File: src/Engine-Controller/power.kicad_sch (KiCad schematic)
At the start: 51 parts, among them P1 EJ508A, P18 PPTC041LFBN-RC, P7 647676-2, U10 LMS8117AMP-3.3_NOPB, U2 LM22672MRE-5.0_NOPB, U3 LMS8117AMP-3.3_NOPB, U6 TPS2115APWR

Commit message: resolved all ERC schematic issues
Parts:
- C5: footprint Engine-Controller:CAP_EEEFP1E151AL -> Engine-Controller:EEEFP1E151AL
- P18: footprint CONN_4840.2201_SCH -> Engine-Controller:PPTC041LFBN-RC
- P7: footprint CONN_2043-1X04G00DAU_OUP -> Engine-Controller:647676-2
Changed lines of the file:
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@@
       (effects (font (size 1.27 1.27)) (justify left))
     )
-    (property "Footprint" "Engine-Controller:CAP_EEEFP1E151AL" (id 2) (at 128.905 52.705 0)
+    (property "Footprint" "Engine-Controller:EEEFP1E151AL" (id 2) (at 128.905 52.705 0)
       (effects (font (size 1.27 1.27)) hide)
     )
@@
     (pin "1")
   )
-  (symbol (lib_id "Engine-Controller:LMS8117AMP-3.3_NOPB") (at 117.475 92.71 0) (unit 1)
+  (symbol (lib_name "LMS8117AMP-3.3_NOPB_1") (lib_id "Engine-Controller:LMS8117AMP-3.3_NOPB") (at 117.475 92.71 0) (unit 1)
     (in_bom yes) (on_board yes)
     (property "Reference" "U3" (id 0) (at 117.475 87.63 0))
@@
       (effects (font (size 1.524 1.524)) hide)
     )
-    (property "Footprint" "CONN_4840.2201_SCH" (id 2) (at 263.525 116.84 0)
+    (property "Footprint" "Engine-Controller:PPTC041LFBN-RC" (id 2) (at 263.525 116.84 0)
       (effects (font (size 1.524 1.524)) hide)
     )
@@
       (effects (font (size 1.524 1.524)) hide)
     )
-    (property "Footprint" "CONN_2043-1X04G00DAU_OUP" (id 2) (at 52.07 180.34 0)
-      (effects (font (size 1.524 1.524)) hide)
-    )
+    (property "Footprint" "Engine-Controller:647676-2" (id 2) (at 52.07 180.34 0)
+      (effects (font (size 1.524 1.524)) hide)
+    )

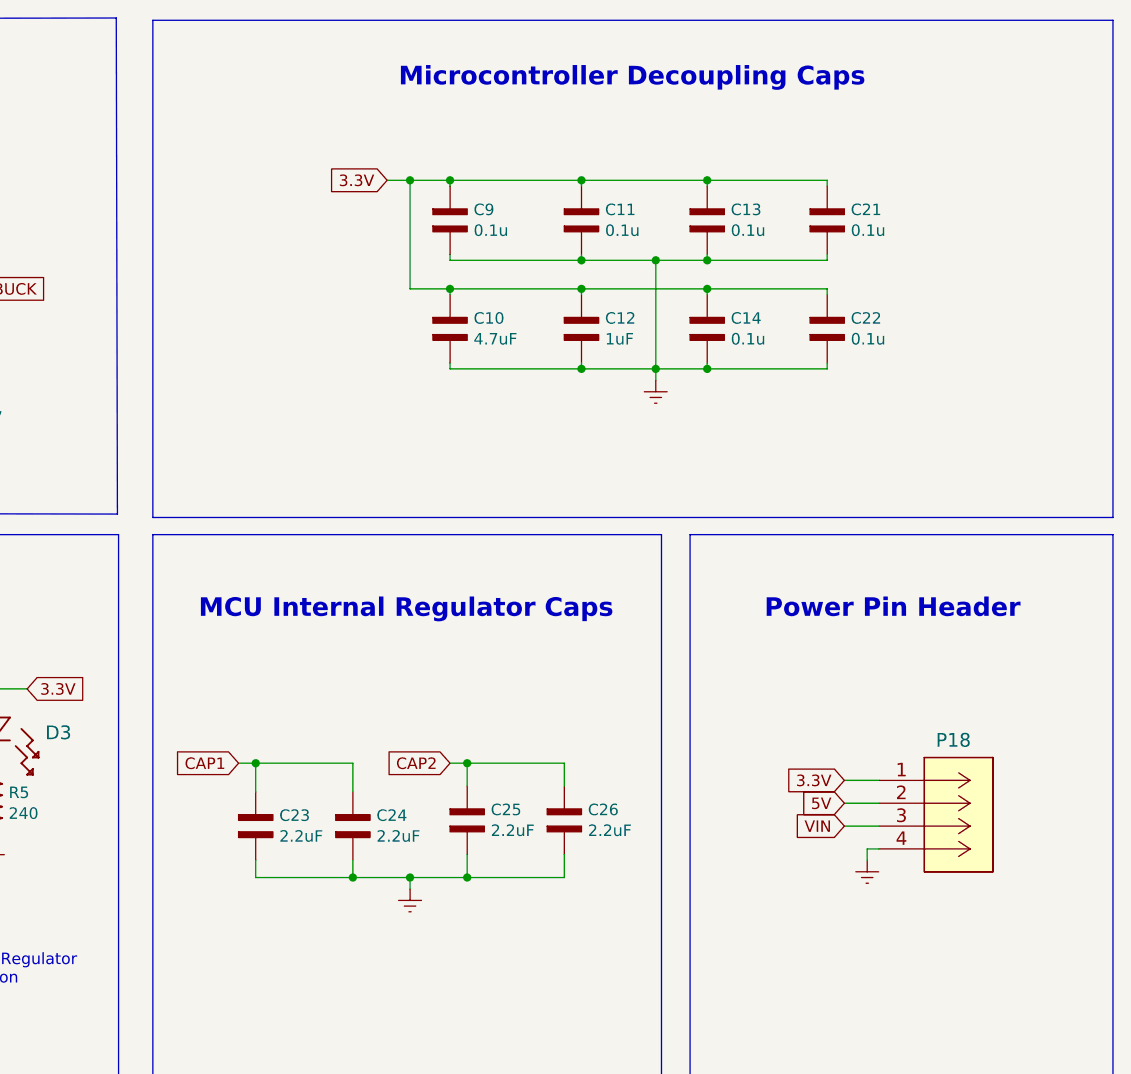
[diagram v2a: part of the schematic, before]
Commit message: removed uncessary caps from MCU LDO pins
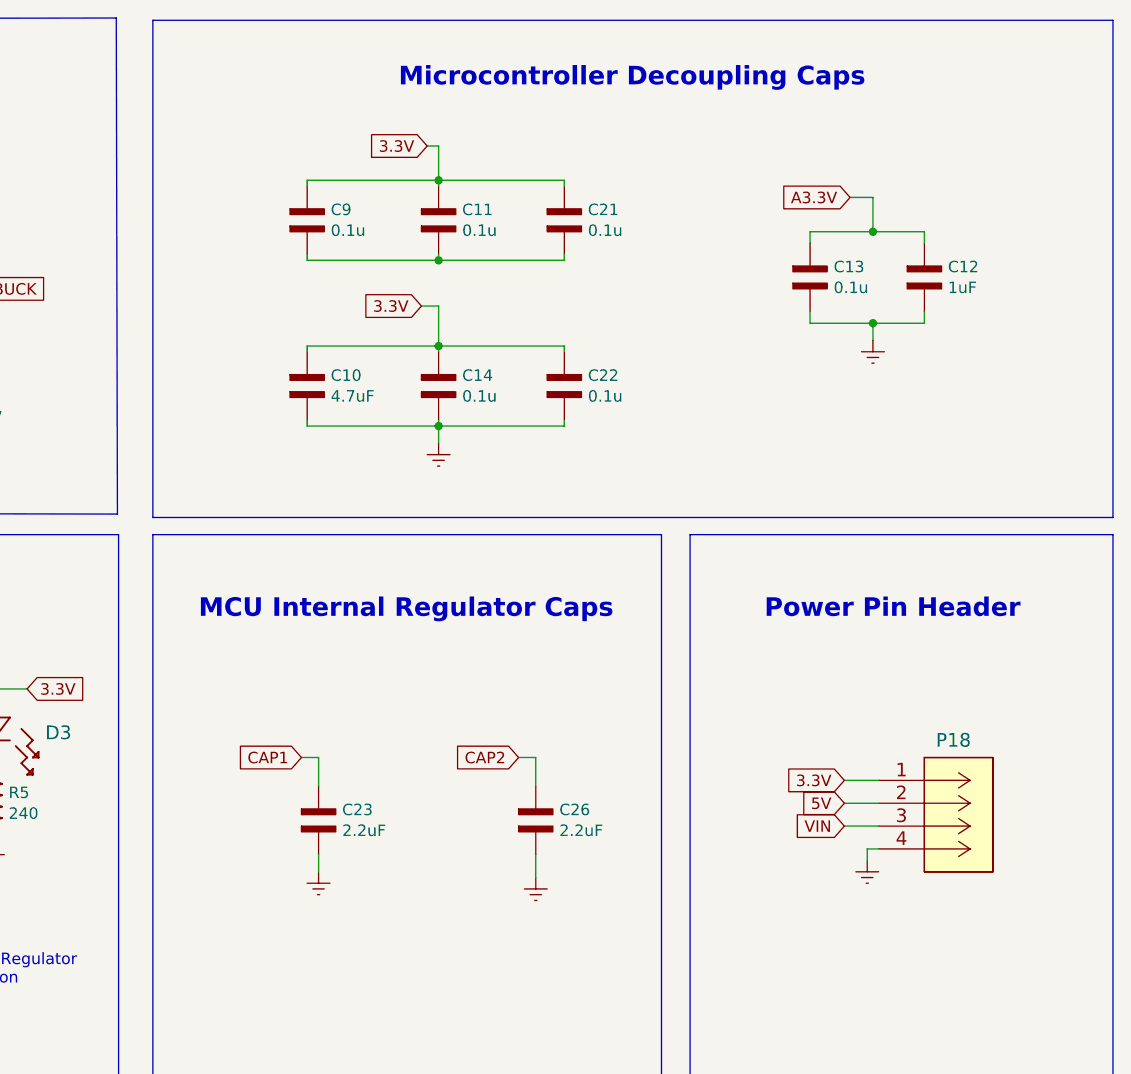
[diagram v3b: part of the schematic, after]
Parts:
- removed C24, C25: 2.2uF, Engine-Controller:CAP_0603, symbol Engine-Controller:CAP_0603
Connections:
- net 3.3V: no longer C12.2, C13.2
- net A3.3V: now also C12.2, C13.2
- net Earth: no longer C11.1, C21.1, C9.1
- new net: C11.1, C21.1, C9.1
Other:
- moved on the sheet: C10, C11, C12, C13, C14, C21, C22, C23, C26, C9

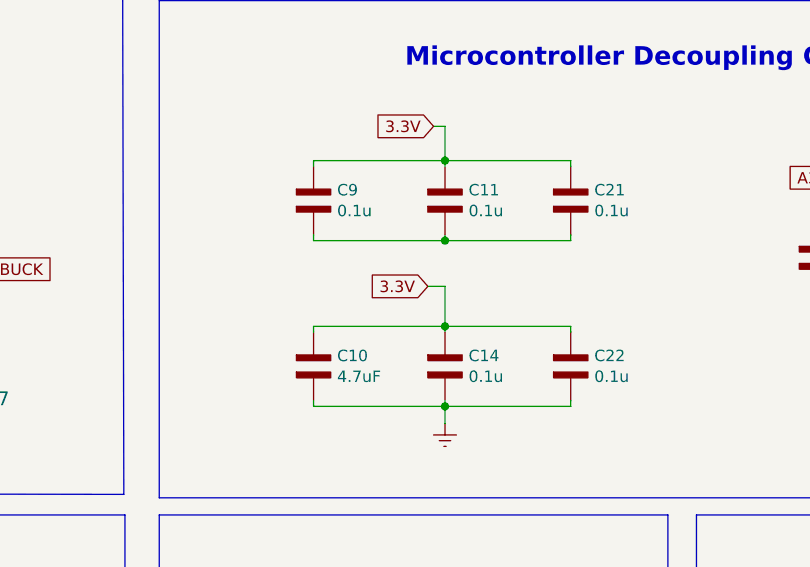
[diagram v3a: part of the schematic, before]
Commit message: removed uneccessary info from footprint lib files
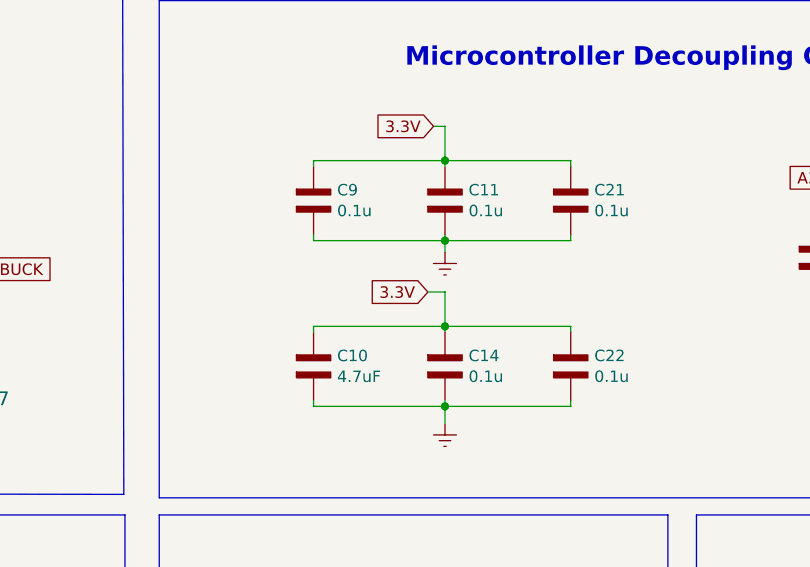
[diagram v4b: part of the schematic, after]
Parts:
- C27, C28, C6, C7: footprint Engine-Controller:CWR11HH106KB -> Engine-Controller:T491A106K010AT
- U10, U3: footprint Engine-Controller:SOT-223 -> Engine-Controller:LMS8117AMP-3.3NOPB
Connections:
- net Earth: now also C11.1, C21.1, C9.1
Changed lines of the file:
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@@
     (stroke (width 0) (type default) (color 0 0 0 0))
   )
-  (wire (pts (xy 202.565 48.895) (xy 204.47 48.895))
+  (wire (pts (xy 202.565 49.53) (xy 204.47 49.53))
     (stroke (width 0) (type default) (color 0 0 0 0))
   )
@@
     (stroke (width 0) (type default) (color 0 0 0 0))
   )
+  (wire (pts (xy 204.47 43.815) (xy 204.47 45.085))
+    (stroke (width 0) (type default) (color 0 0 0 0))
+  )
   (wire (pts (xy 35.052 107.315) (xy 43.18 107.315))
     (stroke (width 0) (type default) (color 0 0 0 0))
@@
     (stroke (width 0) (type default) (color 0 0 0 0))
   )
-  (wire (pts (xy 204.47 48.895) (xy 204.47 53.34))
+  (wire (pts (xy 204.47 49.53) (xy 204.47 53.34))
     (stroke (width 0) (type default) (color 0 0 0 0))
   )
@@
     )
   )
-  (global_label "3.3V" (shape input) (at 202.565 48.895 180) (fields_autoplaced)
-    (effects (font (size 1.27 1.27)) (justify right))
-    (property "Intersheet References" "${INTERSHEET_REFS}" (id 0) (at 132.08 20.32 0)
+  (global_label "3.3V" (shape input) (at 202.565 49.53 180) (fields_autoplaced)
+    (effects (font (size 1.27 1.27)) (justify right))
+    (property "Intersheet References" "${INTERSHEET_REFS}" (id 0) (at 132.08 20.955 0)
       (effects (font (size 1.27 1.27)) hide)
     )
@@
       (effects (font (size 1.524 1.524)) (justify left))
     )
-    (property "Footprint" "Engine-Controller:CWR11HH106KB" (id 2) (at 98.171 95.885 0)
+    (property "Footprint" "Engine-Controller:T491A106K010AT" (id 2) (at 98.171 95.885 0)
       (effects (font (size 1.524 1.524)) hide)
     )
@@
       (effects (font (size 1.524 1.524)) (justify left))
     )
-    (property "Footprint" "Engine-Controller:CWR11HH106KB" (id 2) (at 119.126 95.885 0)
+    (property "Footprint" "Engine-Controller:T491A106K010AT" (id 2) (at 119.126 95.885 0)
       (effects (font (size 1.524 1.524)) hide)
     )
@@
     (pin "1")
   )
-  (symbol (lib_name "LMS8117AMP-3.3_NOPB_1") (lib_id "Engine-Controller:LMS8117AMP-3.3_NOPB") (at 117.475 92.71 0) (unit 1)
+  (symbol (lib_id "Engine-Controller:LMS8117AMP-3.3_NOPB") (at 117.475 92.71 0) (unit 1)
     (in_bom yes) (on_board yes)
     (property "Reference" "U3" (id 0) (at 117.475 87.63 0))
@@
       (effects (font (size 1.27 1.27)) hide)
     )
-    (property "Footprint" "Engine-Controller:SOT-223" (id 2) (at 117.475 92.71 0)
+    (property "Footprint" "Engine-Controller:LMS8117AMP-3.3NOPB" (id 2) (at 117.475 92.71 0)
       (effects (font (size 1.27 1.27)) hide)
     )
@@
     )
     (property "Datasheet" "" (id 3) (at 252.095 110.49 0)
+      (effects (font (size 1.27 1.27)) hide)
+    )
+    (pin "1")
+  )
+  (symbol (lib_id "Engine-Controller:Earth") (at 204.47 45.085 0) (unit 1)
+    (in_bom yes) (on_board yes)
+    (property "Reference" "#PWR0111" (id 0) (at 204.47 51.435 0)
+      (effects (font (size 1.27 1.27)) hide)
+    )
+    (property "Value" "Earth" (id 1) (at 204.47 48.895 0)
+      (effects (font (size 1.27 1.27)) hide)
+    )
+    (property "Footprint" "" (id 2) (at 204.47 45.085 0)
+      (effects (font (size 1.27 1.27)) hide)
+    )
+    (property "Datasheet" "" (id 3) (at 204.47 45.085 0)
       (effects (font (size 1.27 1.27)) hide)
     )
@@
       (effects (font (size 1.524 1.524)) (justify left))
     )
-    (property "Footprint" "Engine-Controller:CWR11HH106KB" (id 2) (at 98.171 118.745 0)
+    (property "Footprint" "Engine-Controller:T491A106K010AT" (id 2) (at 98.171 118.745 0)
       (effects (font (size 1.524 1.524)) hide)
     )
@@
       (effects (font (size 1.27 1.27)) hide)
     )
-    (property "Footprint" "Engine-Controller:SOT-223" (id 2) (at 117.475 115.57 0)
+    (property "Footprint" "Engine-Controller:LMS8117AMP-3.3NOPB" (id 2) (at 117.475 115.57 0)
       (effects (font (size 1.27 1.27)) hide)
     )
@@
       (effects (font (size 1.524 1.524)) (justify left))
     )
-    (property "Footprint" "Engine-Controller:CWR11HH106KB" (id 2) (at 119.126 118.745 0)
+    (property "Footprint" "Engine-Controller:T491A106K010AT" (id 2) (at 119.126 118.745 0)
       (effects (font (size 1.524 1.524)) hide)
     )
@@
   (symbol (lib_id "Engine-Controller:Earth") (at 191.135 111.76 0) (unit 1)
     (in_bom yes) (on_board yes)
-    (property "Reference" "#PWR?" (id 0) (at 191.135 118.11 0)
+    (property "Reference" "#PWR0110" (id 0) (at 191.135 118.11 0)
       (effects (font (size 1.27 1.27)) hide)
     )
@@
   (symbol (lib_id "Engine-Controller:Earth") (at 252.73 52.705 0) (unit 1)
     (in_bom yes) (on_board yes)
-    (property "Reference" "#PWR?" (id 0) (at 252.73 59.055 0)
-      (effects (font (size 1.27 1.27)) hide)
-    )
+    (property "Reference" "#PWR0102" (id 0) (at 252.73 59.055 0)
+      (effects (font (size 1.27 1.27)) hide)
+    )

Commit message: minor lib file changes
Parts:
- C11, C13, C14, C21, C22, C9: value 0.1u -> 0.1uF
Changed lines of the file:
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@@
       (effects (font (size 1.27 1.27)) (justify left))
     )
-    (property "Value" "0.1u" (id 1) (at 221.0562 58.928 90)
+    (property "Value" "0.1uF" (id 1) (at 221.0562 58.928 90)
       (effects (font (size 1.27 1.27)) (justify left))
     )
@@
       (effects (font (size 1.27 1.27)) (justify left))
     )
-    (property "Value" "0.1u" (id 1) (at 192.4812 40.513 90)
+    (property "Value" "0.1uF" (id 1) (at 192.4812 40.513 90)
       (effects (font (size 1.27 1.27)) (justify left))
     )
@@
       (effects (font (size 1.27 1.27)) (justify left))
     )
-    (property "Value" "0.1u" (id 1) (at 207.0862 40.513 90)
+    (property "Value" "0.1uF" (id 1) (at 207.0862 40.513 90)
       (effects (font (size 1.27 1.27)) (justify left))
     )
@@
       (effects (font (size 1.27 1.27)) (justify left))
     )
-    (property "Value" "0.1u" (id 1) (at 207.0862 58.928 90)
+    (property "Value" "0.1uF" (id 1) (at 207.0862 58.928 90)
       (effects (font (size 1.27 1.27)) (justify left))
     )
@@
       (effects (font (size 1.27 1.27)) (justify left))
     )
-    (property "Value" "0.1u" (id 1) (at 221.0562 40.513 90)
+    (property "Value" "0.1uF" (id 1) (at 221.0562 40.513 90)
       (effects (font (size 1.27 1.27)) (justify left))
     )
@@
       (effects (font (size 1.27 1.27)) (justify left))
     )
-    (property "Value" "0.1u" (id 1) (at 248.3612 46.863 90)
-      (effects (font (size 1.27 1.27)) (justify left))
-    )
+    (property "Value" "0.1uF" (id 1) (at 248.3612 46.863 90)
+      (effects (font (size 1.27 1.27)) (justify left))
+    )

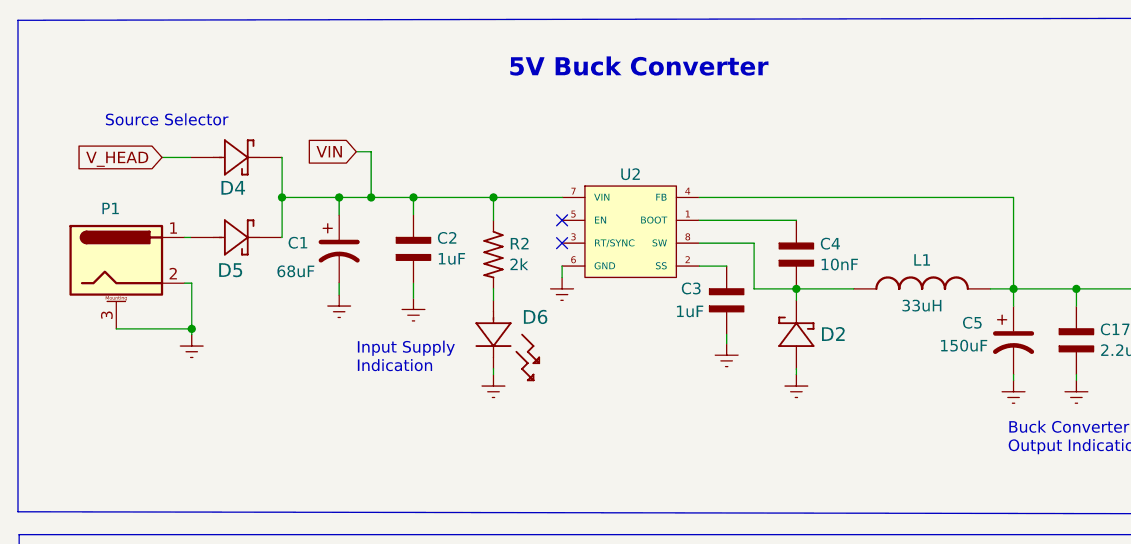
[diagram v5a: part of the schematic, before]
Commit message: created rev5 schematic, added USB detection, updated PT readout circuits
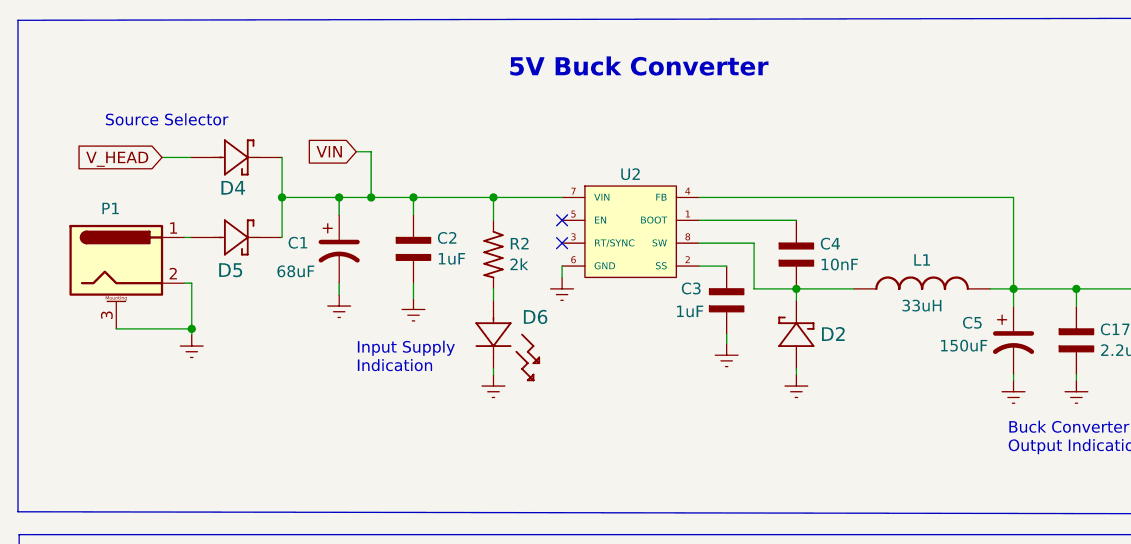
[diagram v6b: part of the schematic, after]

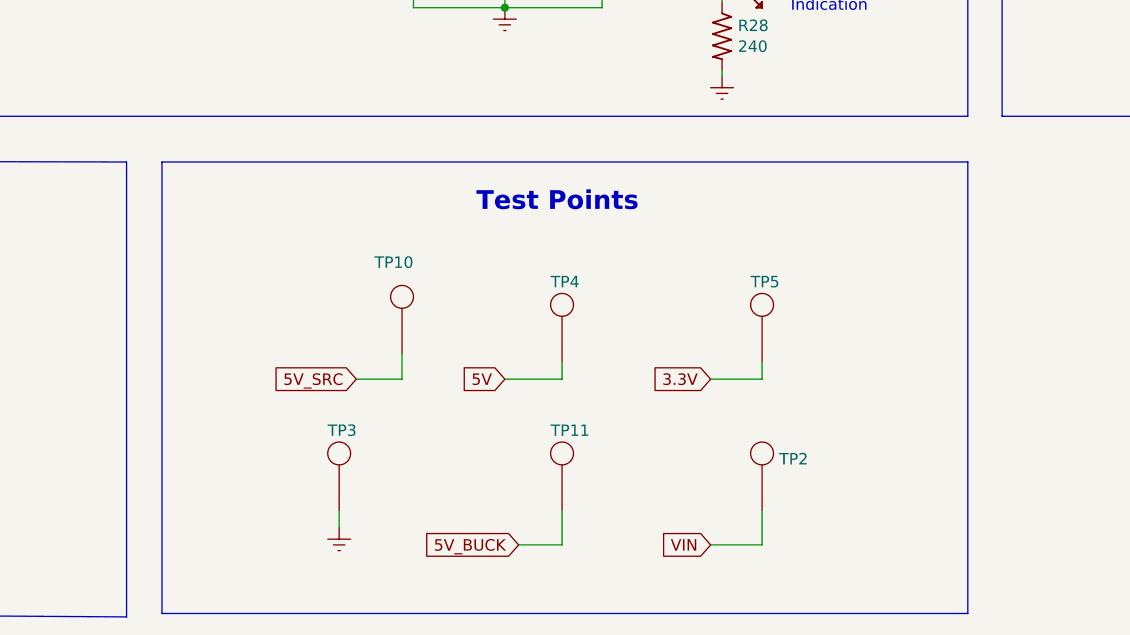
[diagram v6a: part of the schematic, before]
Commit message: removed wireless interface connector
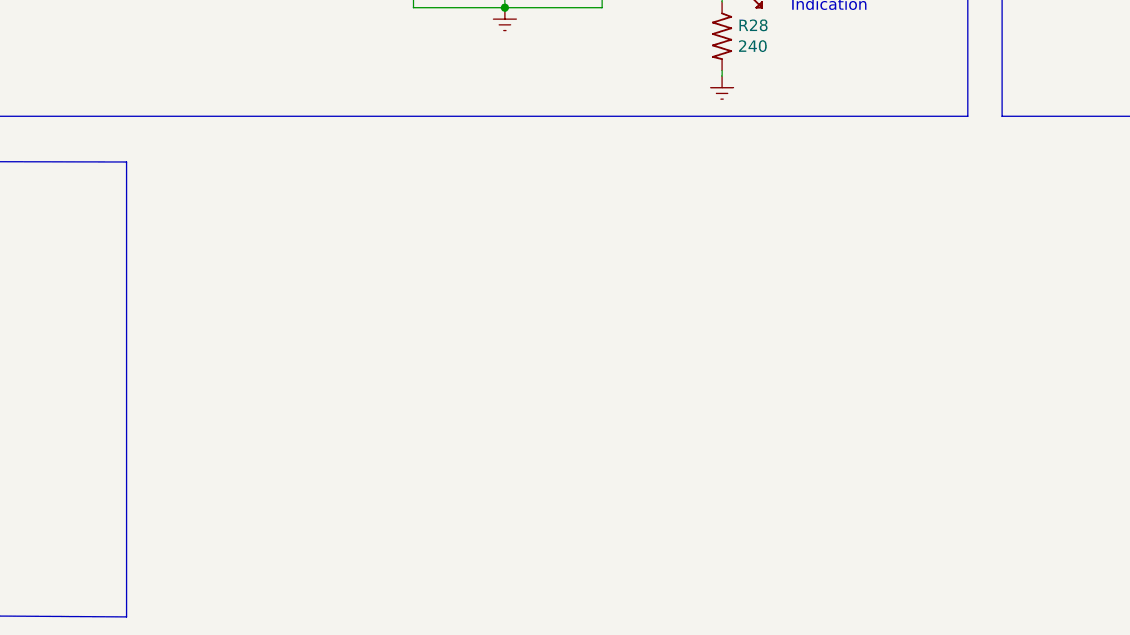
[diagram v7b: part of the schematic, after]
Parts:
- removed TP10, TP11: TP, Engine-Controller:TP, symbol Engine-Controller:TP
- removed TP2: TPVIN, Engine-Controller:TP, symbol Engine-Controller:TP
- removed TP3: TPGND, Engine-Controller:TP, symbol Engine-Controller:TP
- removed TP4: TP5V, Engine-Controller:TP, symbol Engine-Controller:TP
- removed TP5: 3.3V, Engine-Controller:TP, symbol Engine-Controller:TP
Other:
- note removed: "Test Points"
